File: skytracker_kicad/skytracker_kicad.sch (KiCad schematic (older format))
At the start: 21 parts, among them M1 28BYJ-48, SW1 HOME_DETECT, SW2 LIM_DETECT, SW3 STATE_SELECT, U1 ULN2003A

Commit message: schematic updates
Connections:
- net at R1.2: now also A1.14 (D11); no longer A1.12 (D9)
- net at R2.1: now also A1.15 (D12); no longer A1.13 (D10)
- net at R3.1: now also A1.16 (D13); no longer A1.14 (D11)
- net M4: now reaches A1.10 (D7), U1.4 (I4)
- net at SW3.1: now also A1.4 (GND), D1.1 (K), D2.1 (K), D3.1 (K), SW1.1, SW2.1, SW3.2, SW3.3; no longer A1.15 (D12)
- net M1: now reaches A1.7 (D4), U1.1 (I1)
- net M2: now reaches A1.8 (D5), U1.2 (I2)
- net M3: now reaches A1.9 (D6), U1.3 (I3)
- net GND: no longer names the net of A1.29 (GND), C1.2, D4.1 (K), D5.1 (K), D6.1 (K), D7.1 (K), U1.8 (GND)
- net GND: no longer A1.4 (GND), D1.1 (K), D2.1 (K), D3.1 (K), SW1.1, SW2.1, SW3.2
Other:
- moved on the sheet: D1, D2, D3, R1, R2, R3, SW1, SW2, SW3

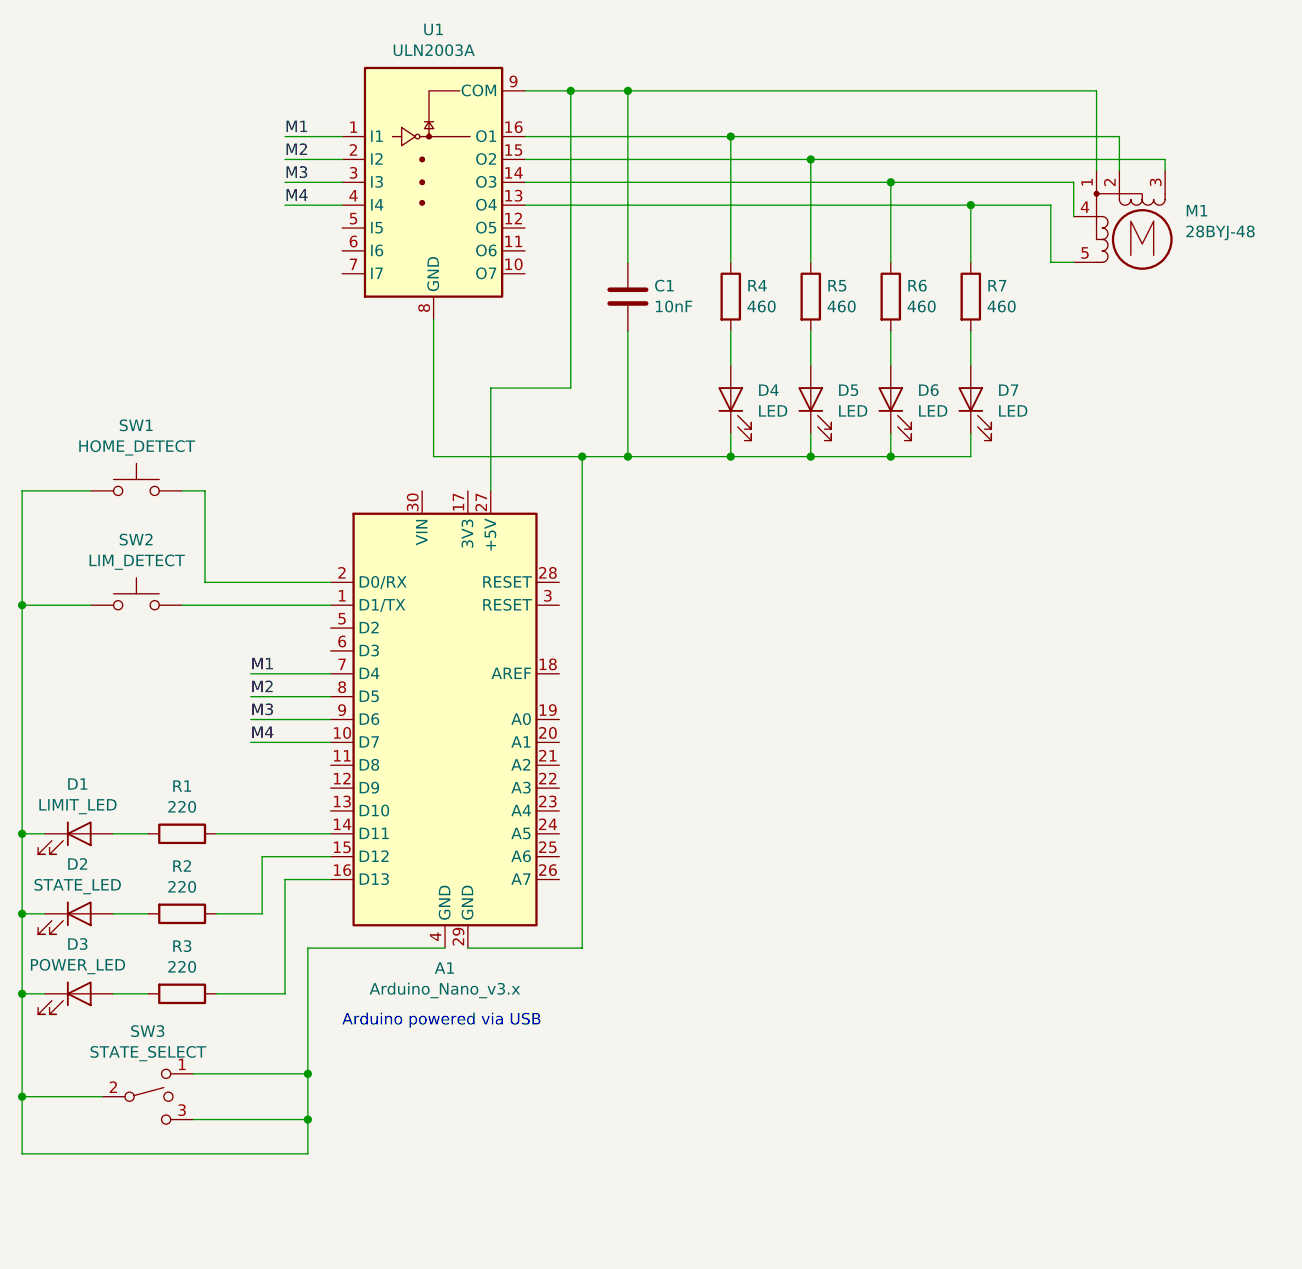
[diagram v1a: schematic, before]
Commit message: Fixed schematic
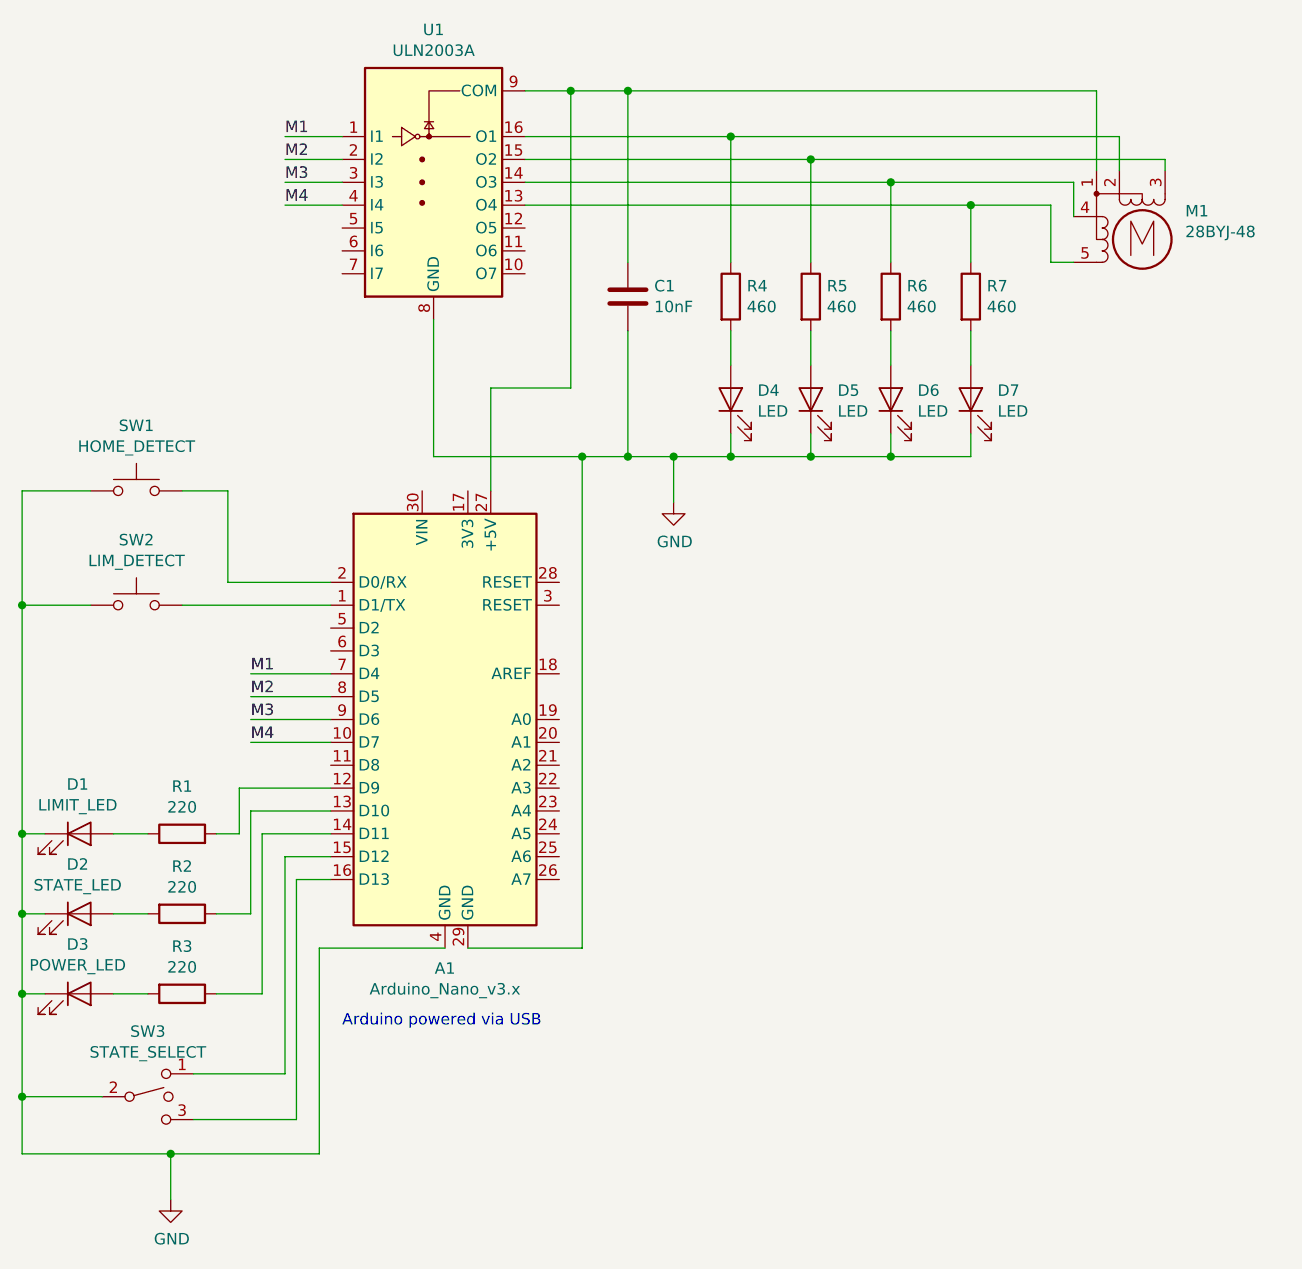
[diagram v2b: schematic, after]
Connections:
- net at R1.2: now also A1.12 (D9); no longer A1.14 (D11)
- net at R2.1: now also A1.13 (D10); no longer A1.15 (D12)
- net at R3.1: now also A1.14 (D11); no longer A1.16 (D13)
- net GND: now reaches A1.29 (GND), C1.2, D4.1 (K), D5.1 (K), D6.1 (K), D7.1 (K), U1.8 (GND)
- net GND: now also A1.4 (GND), D1.1 (K), D2.1 (K), D3.1 (K), SW1.1, SW2.1, SW3.2
- new net: A1.15 (D12), SW3.1
- new net: A1.16 (D13), SW3.3
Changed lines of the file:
@@
 EESchema Schematic File Version 4
+LIBS:skytracker_kicad-cache
 EELAYER 30 0
 EELAYER END
@@
 Wire Wire Line
 	3550 5700 3550 6150
-Wire Wire Line
-	3550 6400 4800 6400
 Connection ~ 3550 6150
 Wire Wire Line
@@
 Wire Wire Line
 	3550 6150 3900 6150
-Wire Wire Line
-	5400 5500 4800 5500
 $Comp
 L Switch:SW_Push SW2
@@
 $EndComp
 Wire Wire Line
-	4250 3500 4350 3500
-Wire Wire Line
-	4350 3500 4350 3900
-Wire Wire Line
-	4350 3900 4900 3900
+	4250 3500 4450 3500
+Wire Wire Line
+	4450 3500 4450 3900
+Wire Wire Line
+	4450 3900 4900 3900
 Wire Wire Line
 	3850 3500 3550 3500
@@
 Arduino powered via USB
 Wire Wire Line
-	6200 3350 6650 3350
-Wire Wire Line
-	4800 5500 4800 6050
-Wire Wire Line
-	4300 6050 4800 6050
-Connection ~ 4800 6050
-Wire Wire Line
-	4800 6050 4800 6250
-Wire Wire Line
-	4300 6250 4800 6250
-Connection ~ 4800 6250
-Wire Wire Line
-	4800 6250 4800 6400
+	6200 3350 6400 3350
+Wire Wire Line
+	4300 6050 4700 6050
 Wire Wire Line
 	3550 4000 3550 5000
@@
 M4
 Wire Wire Line
-	4900 5200 4700 5200
-Wire Wire Line
-	4700 5200 4700 5700
-Wire Wire Line
-	4700 5700 4400 5700
-Wire Wire Line
-	4400 5350 4600 5350
-Wire Wire Line
-	4600 5350 4600 5100
-Wire Wire Line
-	4600 5100 4900 5100
-Wire Wire Line
-	4400 5000 4900 5000
+	4400 5700 4600 5700
+Wire Wire Line
+	4600 5700 4600 5000
+Wire Wire Line
+	4600 5000 4900 5000
+Wire Wire Line
+	4400 5000 4500 5000
+Wire Wire Line
+	4500 5000 4500 4800
+Wire Wire Line
+	4500 4800 4900 4800
+Wire Wire Line
+	4400 5350 4550 5350
+Wire Wire Line
+	4550 5350 4550 4900
+Wire Wire Line
+	4550 4900 4900 4900
+Wire Wire Line
+	4900 5100 4700 5100
+Wire Wire Line
+	4700 5100 4700 6050
+Wire Wire Line
+	4300 6250 4750 6250
+Wire Wire Line
+	4900 5200 4750 5200
+Wire Wire Line
+	4750 5200 4750 6250
+Wire Wire Line
+	4850 6400 4850 5500
+Wire Wire Line
+	4850 5500 5400 5500
+Wire Wire Line
+	3550 6400 4200 6400
+$Comp
+L power:GND #PWR?
+U 1 1 5DAEAA02
+P 4200 6600
+F 0 "#PWR?" H 4200 6350 50  0001 C CNN
+F 1 "GND" H 4205 6427 50  0000 C CNN
+F 2 "" H 4200 6600 50  0001 C CNN
+F 3 "" H 4200 6600 50  0001 C CNN
+	1    4200 6600
+	1    0    0    -1
+$EndComp
+Wire Wire Line
+	4200 6600 4200 6400
+Connection ~ 4200 6400
+Wire Wire Line
+	4200 6400 4850 6400
+$Comp
+L power:GND #PWR?
+U 1 1 5DAEDE1E
+P 6400 3550
+F 0 "#PWR?" H 6400 3300 50  0001 C CNN
+F 1 "GND" H 6405 3377 50  0000 C CNN
+F 2 "" H 6400 3550 50  0001 C CNN
+F 3 "" H 6400 3550 50  0001 C CNN
+	1    6400 3550
+	1    0    0    -1
+$EndComp
+Wire Wire Line
+	6400 3550 6400 3350
+Connection ~ 6400 3350
+Wire Wire Line
+	6400 3350 6650 3350
 $EndSCHEMATC
